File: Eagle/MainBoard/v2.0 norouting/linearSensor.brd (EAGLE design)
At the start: 41.9 x 30.7 mm, 21 parts, among them CON1 SPI, X3 16MHz, X4 MINI-USB

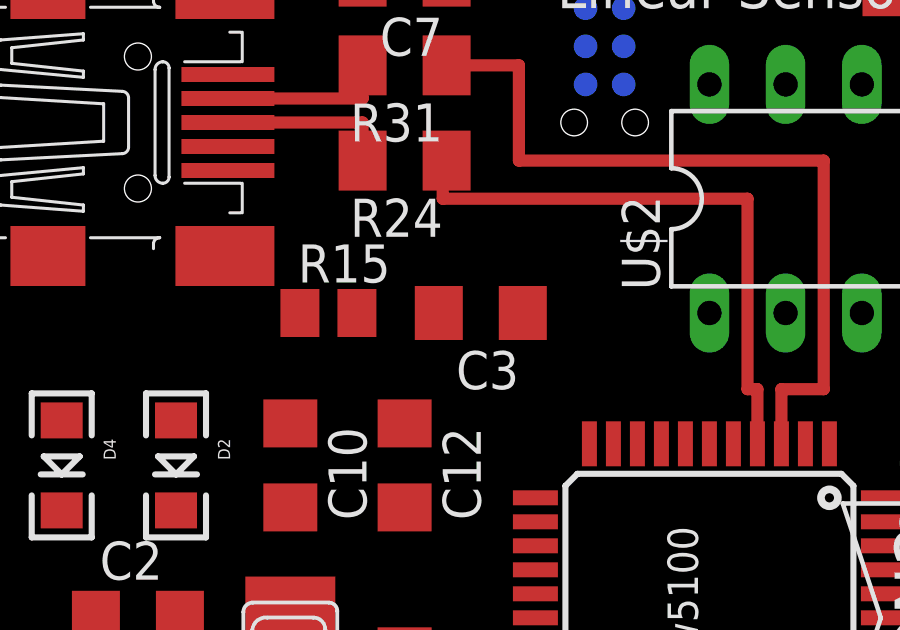
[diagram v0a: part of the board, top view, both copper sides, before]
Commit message: Refactor the code to allow more possibilities Show linearity of the detector
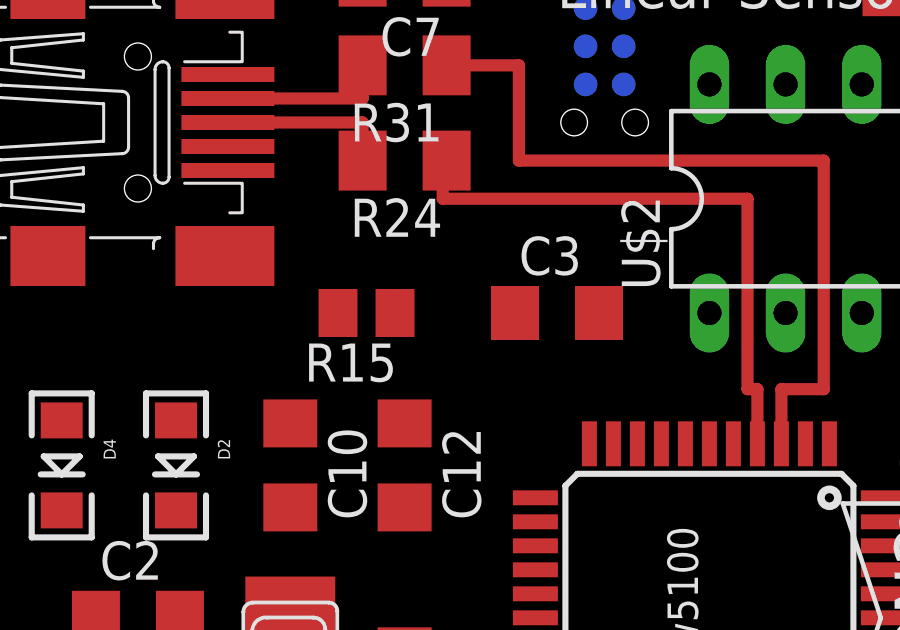
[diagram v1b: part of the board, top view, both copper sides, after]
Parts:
- moved C3 2.54 mm to (19.1, 17.8), turned to 0 degrees
- moved R15 1.27 mm to (12.7, 17.8), turned to 180 degrees
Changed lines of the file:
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@@
 <attribute name="VALUE" x="32.3215" y="7.366" size="1.27" layer="27" rot="R270"/>
 </element>
-<element name="R15" library="resistor" package="M0805" value="10k" x="11.43" y="17.78" smashed="yes">
-<attribute name="NAME" x="10.414" y="18.796" size="1.27" layer="25"/>
-<attribute name="VALUE" x="12.954" y="17.399" size="1.27" layer="27"/>
-</element>
-<element name="C3" library="rcl" package="C1206" value="100nF" x="16.51" y="17.78" rot="R180"/>
+<element name="R15" library="resistor" package="M0805" value="10k" x="12.7" y="17.78" smashed="yes" rot="R180">
+<attribute name="NAME" x="13.716" y="16.764" size="1.27" layer="25" rot="R180"/>
+<attribute name="VALUE" x="11.176" y="18.161" size="1.27" layer="27" rot="R180"/>
+</element>
+<element name="C3" library="rcl" package="C1206" value="100nF" x="19.05" y="17.78"/>
 <element name="X3" library="lpatiny" package="NX6035" value="16MHz" x="10.16" y="5.08" smashed="yes" rot="R90">
 <attribute name="NAME" x="7.36" y="2.38" size="1.27" layer="25" font="vector" rot="R90"/>
@@
 <wire x1="13.97" y1="14.1" x2="18.33" y2="9.22" width="0" layer="19" extent="1-1"/>
 <wire x1="10.16" y1="14.1" x2="13.97" y2="14.1" width="0" layer="19" extent="1-1"/>
-<wire x1="17.91" y1="17.78" x2="13.97" y2="14.1" width="0" layer="19" extent="1-1"/>
+<wire x1="17.65" y1="17.78" x2="13.97" y2="14.1" width="0" layer="19" extent="1-1"/>
 <wire x1="20.13" y1="1.82" x2="18.33" y2="9.22" width="0" layer="19" extent="1-1"/>
-<wire x1="20.0025" y1="25.4" x2="17.91" y2="17.78" width="0" layer="19" extent="1-16"/>
+<wire x1="20.0025" y1="25.4" x2="17.65" y2="17.78" width="0" layer="19" extent="1-16"/>
 <wire x1="15.37" y1="28.8925" x2="20.0025" y2="25.4" width="0" layer="19" extent="1-16"/>
 <wire x1="8.08" y1="22.53" x2="10.16" y2="14.1" width="0" layer="19" extent="1-1"/>
@@
 <contactref element="U$4" pad="6"/>
 <contactref element="C3" pad="2"/>
-<wire x1="15.11" y1="17.78" x2="24.13" y2="13.42" width="0" layer="19" extent="1-1"/>
+<wire x1="24.13" y1="13.42" x2="20.45" y2="17.78" width="0" layer="19" extent="1-1"/>
 </signal>
 <signal name="D12*">
@@
 <wire x1="6.35" y1="11.2" x2="10.16" y2="11.3" width="0" layer="19" extent="1-1"/>
 <wire x1="2.54" y1="11.2" x2="6.35" y2="11.2" width="0" layer="19" extent="1-1"/>
-<wire x1="12.38" y1="17.78" x2="13.97" y2="11.3" width="0" layer="19" extent="1-1"/>
+<wire x1="11.75" y1="17.78" x2="10.16" y2="11.3" width="0" layer="19" extent="1-1"/>
 </signal>
 <signal name="D8*">
@@
 <contactref element="R15" pad="1"/>
 <contactref element="CON1" pad="RESET"/>
-<wire x1="10.48" y1="17.78" x2="21.2725" y2="25.4" width="0" layer="19" extent="1-16"/>
-<wire x1="18.33" y1="10.82" x2="10.48" y2="17.78" width="0" layer="19" extent="1-1"/>
+<wire x1="13.65" y1="17.78" x2="21.2725" y2="25.4" width="0" layer="19" extent="1-16"/>
+<wire x1="18.33" y1="10.82" x2="13.65" y2="17.78" width="0" layer="19" extent="1-1"/>
 </signal>
 </signals>
